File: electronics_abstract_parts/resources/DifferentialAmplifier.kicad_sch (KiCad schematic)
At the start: 5 parts

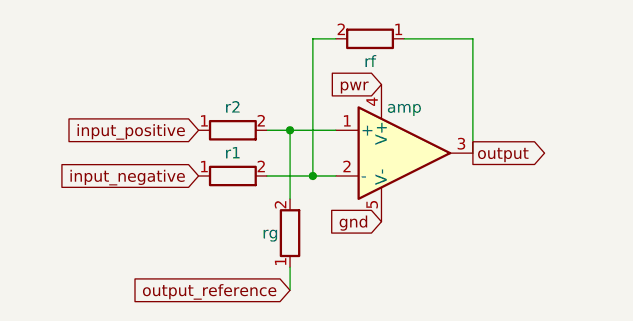
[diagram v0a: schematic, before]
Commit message: Add analog signal range modeling (#298)
voltage_out now means the voltage the device is capable of generating
(even as an unintended transient), while signal_out is the voltage the
device generates under normal operating conditions. voltage_limit now
refers the maximum operating condition (sometimes the absolute maximum
rating), while signal_limit is the functional operating limit (which may
differ from the maximum rating, e.g. for a non-RRIO opamp or weirder
ADCs - looking at you ESP32). Basically adds automated checking for
those edge cases.

Updates all part models with signal modelling.

Other changes:
- Enforce voltage_limits for AnalogLinks - apparently the assertion was
missing before...
- Updates the compiler to handle RangeEmpty in additions and
multiplications.
- Add AnalogClampZenerDiode, to clamp analog voltage
- Clean up some of the analog port definitions
- Add ResistiveDivider.divider_output and divider_ratio utility to share
these common calculation functions

Future things to do:
- Generate the proper signal output range for opamp amplifiers and
diffamps - currently it's intersected with the amp output range to avoid
excessive large ranges as a result of input tolerances.
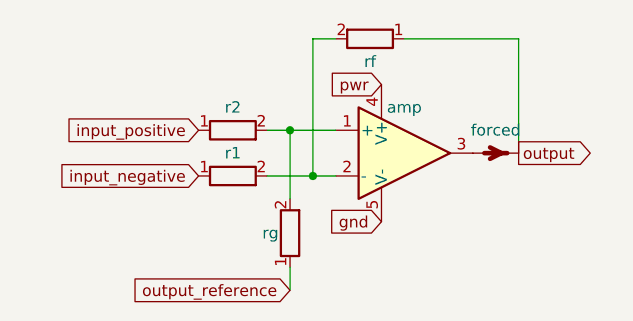
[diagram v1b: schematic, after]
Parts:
- added forced: ~, symbol edg_importable:Adapter
- amp: value ~ -> (none); Spice_Netlist_Enabled Y -> (none); Spice_Primitive X -> (none)
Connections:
- net output: now also forced.2; no longer amp.3
- new net: amp.3, forced.1

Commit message: Continued example boards (#299)
More example boards:
- IoT soldering iron controller with discrete synchronous buck converter
- Update the IoT fan controller with a discrete micro (instead of RF
module)
- Picoprobe, maybe this will be the RP2040 board that finally works
- USB key, as an example of an ultra-size-optimized board
- Jacdac mechanical keyswitch

Including these additional libraries:
- CombinedCapacitor as a multipack device, to combine capacitors on the
same net
- Half-bridge with gate driver, replacing the old half-bridge generator
which didn't work
- HDC1080 I2C temperature sensor
- UCC27282 gate driver, 5v compatible with shoot through protect
- JLC caps: allow bypassing capacitance-based minimum package size
- JLC crystals: add 2520 sized crystal
- JLC switch FET: add manual gate charge
- 0404 RGB LED
- LP5907: X2SON version
- L78Lxx high(er) votlage regulator
- ESP32C3 (raw chip) microcontroller, plus support for opt-in use of
strapping pins
- ESP32S3: opt-in for GPIO0 strapping pin
- Refactor IoController _make_export_vector for better composability, to
support remapping strapping pins in the wrapper block
- STM32G031 and STM32L432 (crystal-less USB!) microcontrollers
- OPA2333 dual (multipacked) precision opamp
- MAX98357A in QFN
- USB-A plug pads (PCB as the plug)

and these infrastructural abstract components / changes:
- abstract antenna
- voltage-source/sink wrapper around inductor for power filtering
- packed opamp element
- TVS diode, including wrappers across power and digital lines
- better definition for gate drivers
- low-pass RC for analog signals
- Pi impedance match filter with unit tests
- Jacdac port and links infrastructure
- simplify some part table parsing regex

and these bugfixes:
- support absolute tolerances (+/-pF) in capacitor table parser
- support optional reset on micros with internal pull resistors, don't
require reset on SWD header (but connected by default)
- plumb through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
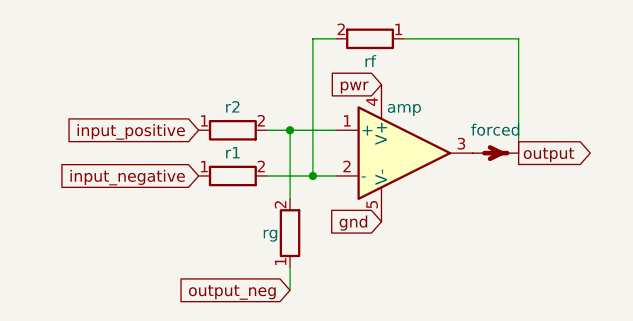
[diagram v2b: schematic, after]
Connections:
- net output_reference renamed output_neg
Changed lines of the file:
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@@
     )
   )
-  (global_label "output_reference" (shape input) (at 114.3 104.14 180) (fields_autoplaced)
+  (global_label "output_neg" (shape input) (at 114.3 104.14 180) (fields_autoplaced)
     (effects (font (size 1.27 1.27)) (justify right))
-    (property "Intersheetrefs" "${INTERSHEET_REFS}" (at 95.9817 104.0606 0)
+    (property "Intersheetrefs" "${INTERSHEET_REFS}" (at 100.9926 104.14 0)
       (effects (font (size 1.27 1.27)) (justify right) hide)
     )
